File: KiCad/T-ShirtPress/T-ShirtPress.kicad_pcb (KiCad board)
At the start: 4 copper layers, 100 x 100 mm, 49 parts, among them J1 ST_LINKV2, J2 Display, J3 Thermistor, J4 SSR_CONTROL, J5 AC_LINE, J6 AC_NEUTRAL, U1 AMS1117-3.3, U2 STM32F429ZGTx, Y1 8MHz

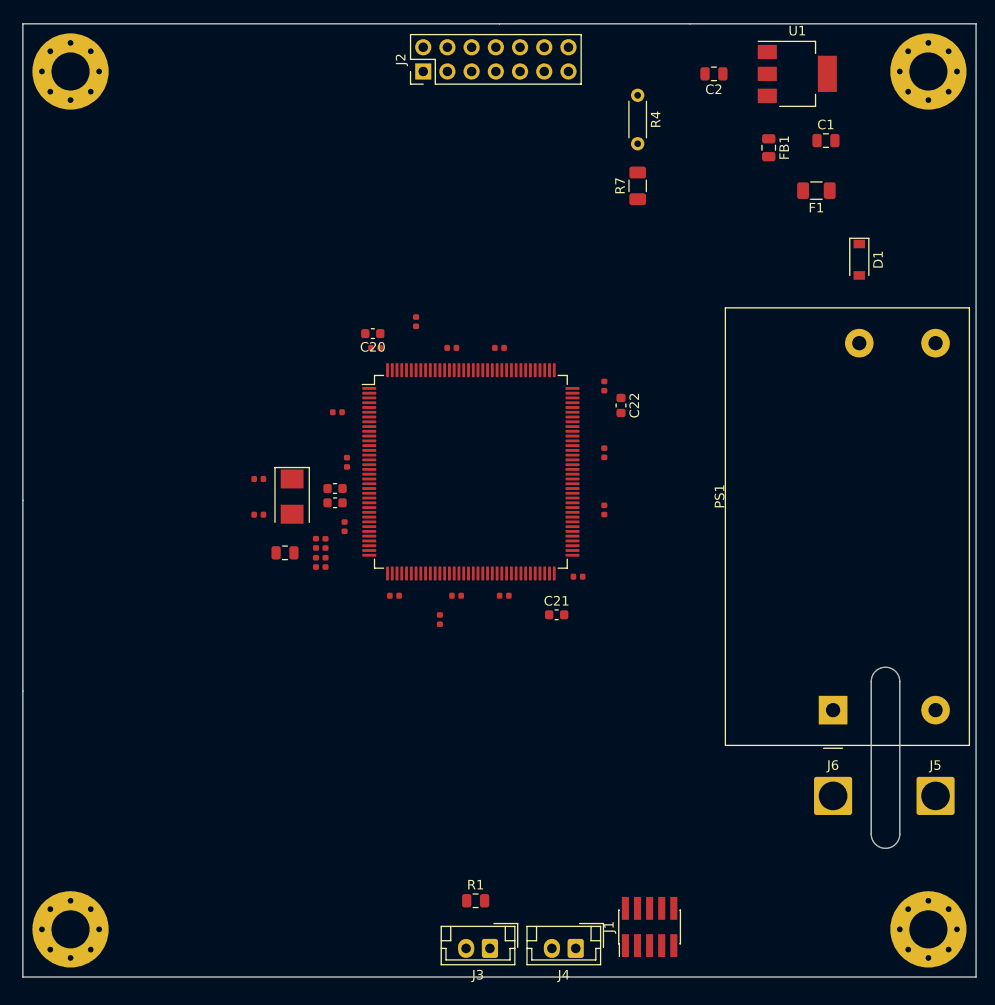
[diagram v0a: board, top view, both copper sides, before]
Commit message: PCB Done!
The pcb should be done now and it is ordered with assembly so hopefully everything goes well and it will arrive in roughly a week.
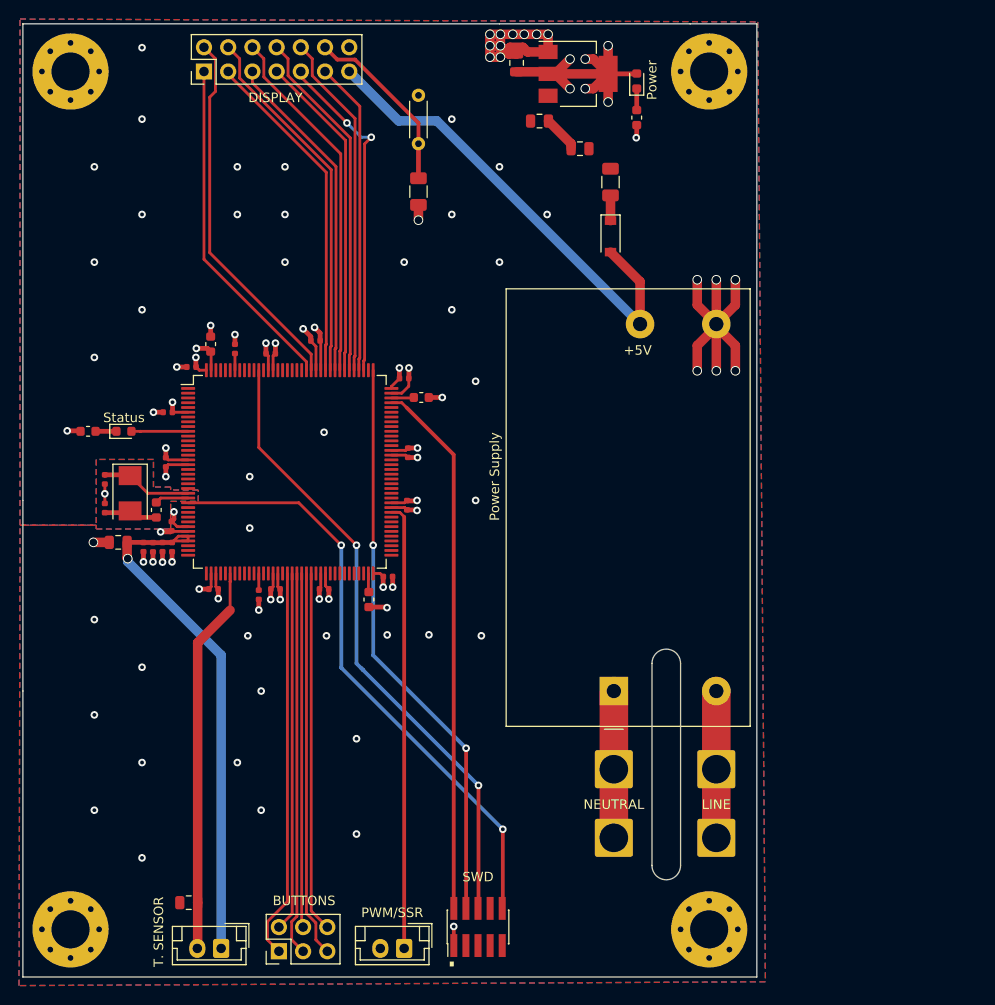
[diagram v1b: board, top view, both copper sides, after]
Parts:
- added G***: LOGO, Logo:logo2, B.Cu at (104.4, 80.9)
- added J7: Buttons, Connector_PinHeader_2.54mm:PinHeader_2x03_P2.54mm_Vertical, F.Cu at (56.9, 127.3)
- added LINE: AC_LINE, Connector_Wire:SolderWire-2.5sqmm_1x01_D2.4mm_OD3.6mm, F.Cu at (102.8, 115.4)
- added NEUTRAL: AC_NEUTRAL, Connector_Wire:SolderWire-2.5sqmm_1x01_D2.4mm_OD3.6mm, F.Cu at (92.0, 115.4)
- added Power: LED_Red, LED_SMD:LED_0603_1608Metric, F.Cu at (94.4, 36.0)
- added R8: 220, Resistor_SMD:R_0603_1608Metric, F.Cu at (94.4, 39.8)
- added Status: LED_Red, LED_SMD:LED_0603_1608Metric, F.Cu at (40.6, 72.8)
- Power Supply: renamed from PS1
- R2: value 0 -> 220
- moved C1 30.1 mm to (84.2, 40.2), turned to 180 degrees
- moved R1 30.1 mm to (47.4, 122.2), turned to 180 degrees
- moved J3 28.2 mm to (50.8, 127.0)
- moved R2 26.6 mm to (36.8, 72.8), turned to 180 degrees
- moved D1 26.2 mm to (91.7, 52.3)
- moved J5 23.2 mm to (102.8, 108.2)
- moved J6 23.2 mm to (92.0, 108.2)
- moved Power Supply 23.1 mm to (92.0, 100.0)
- moved R7 23.0 mm to (71.5, 47.6), turned to 270 degrees
- moved H1 23.0 mm to (102.0, 125.0)
- moved H2 23.0 mm to (102.0, 35.0)
- moved J2 23.0 mm to (49.0, 35.0)
- moved R4 23.0 mm to (71.5, 37.5)
- moved U1 23.0 mm to (88.2, 35.2)
- moved F1 21.6 mm to (91.7, 46.6), turned to 90 degrees
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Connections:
- C23 pad 1: Net-(C23-Pad1) -> HSE_IN
- R2 pad 1: Net-(C23-Pad1) -> Net-(D2-Pad1)
- R2 pad 2: HSE_IN -> GND
- U2 pad 54: Net-(U2-Pad54) -> BUTTON_ON
- U2 pad 55: Net-(U2-Pad55) -> BUTTON_GO
- U2 pad 56: Net-(U2-Pad56) -> BUTTON_TEMP_UP
- U2 pad 57: Net-(U2-Pad57) -> BUTTON_TEMP_DOWN
- U2 pad 58: Net-(U2-Pad58) -> BUTTON_TIME_UP
- U2 pad 59: Net-(U2-Pad59) -> BUTTON_TIME_DOWN
- Y1 pad 1: Net-(C23-Pad1) -> HSE_IN
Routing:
- net GND: track 0.00 -> 107.9 mm, vias 0 -> 82
- net +3V3: track 0.00 -> 75.3 mm, vias 0 -> 22
- net SWO: track 0.00 -> 66.3 mm, vias 0 -> 2
- net NRST: track 0.00 -> 63.1 mm, vias 0 -> 2
- net SWCLK: track 0.00 -> 60.5 mm, vias 0 -> 2
- net SWDIO: track 0.00 -> 56.9 mm
- net +3.3VA: track 0.00 -> 55.6 mm, vias 0 -> 1
- net +5V: track 0.00 -> 50.3 mm
- net PWM: track 0.00 -> 46.8 mm
- net BUTTON_ON: track 0.00 -> 41.0 mm
- net V_TEMP: track 0.00 -> 40.8 mm
- net BUTTON_TIME_UP: track 0.00 -> 40.5 mm
- net BUTTON_TEMP_UP: track 0.00 -> 40.4 mm
- net D6: track 0.00 -> 39.0 mm
- net D4: track 0.00 -> 38.4 mm
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- added copper zone on VCC.Cu, net +3V3
- added copper zone on B.Cu, net GND
- added copper zone on F.Cu, net GND
- added copper zone on GND.Cu, net GND
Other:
- board size 100 x 100 mm -> 77 x 100 mm
- board text added: "+5"
- board text added: "+5V"
- board text added: "."
- board text added: "0-1"
- board text added: "2-3"
- board text added: "4-5"
- board text added: "6-7"
- board text added: "BUTTONS"
- board text added: "CONT-RS"
- board text added: "DISPLAY"
- board text added: "GND"
- board text added: "ON-GO"
- board text added: "PWM"
- board text added: "PWM/SSR"
- board text added: "RW-EN"
- board text added: "SWD"
- board text added: "T. SENSOR"
- board text added: "Temp Up-Down"
- board text added: "Time, Up-Down"

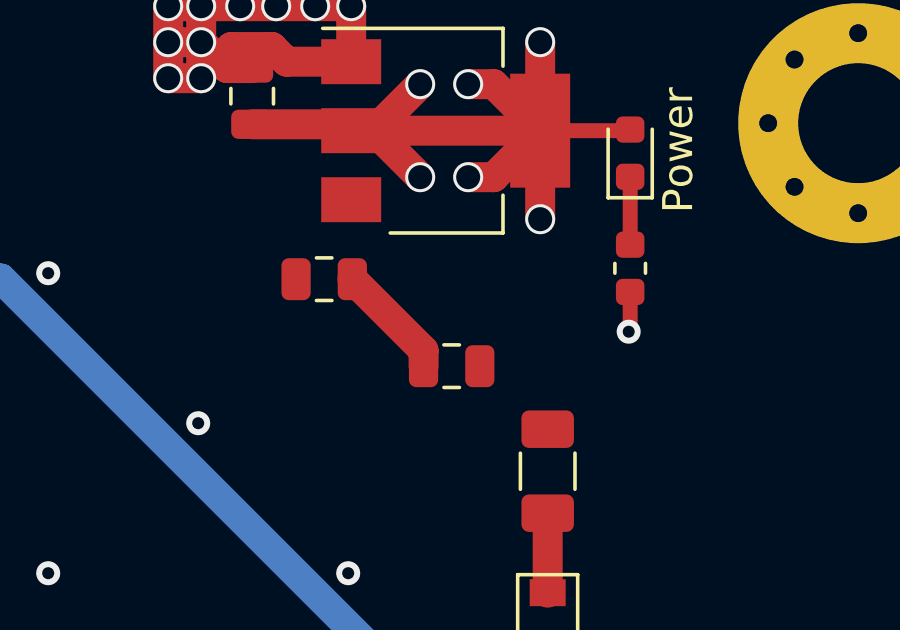
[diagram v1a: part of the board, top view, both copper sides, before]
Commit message: Fixed error with PCB layout
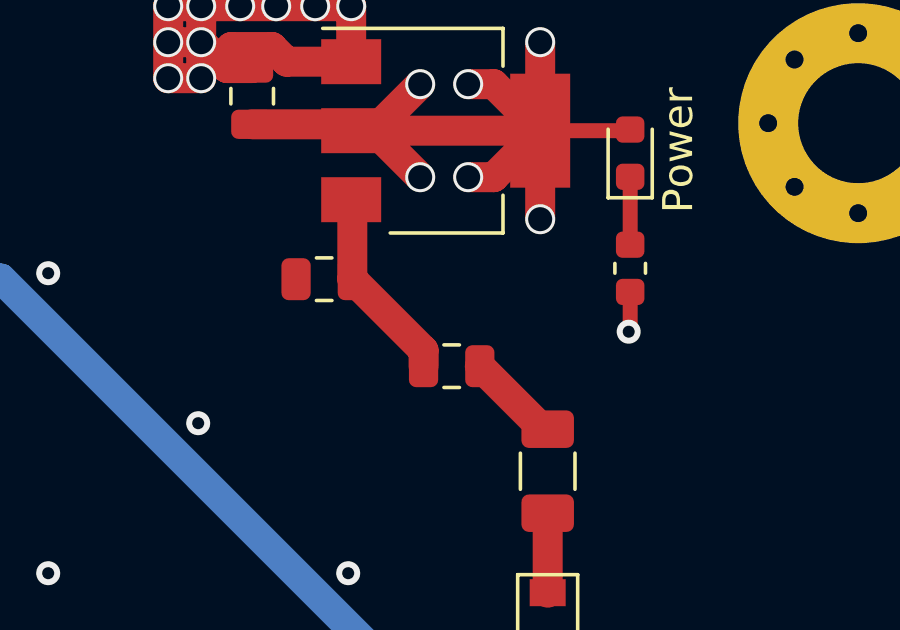
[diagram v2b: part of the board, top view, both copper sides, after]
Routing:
- net Net-(F1-Pad2): track 0.00 -> 3.13 mm
- net Net-(C1-Pad1): track 3.94 -> 6.55 mm
